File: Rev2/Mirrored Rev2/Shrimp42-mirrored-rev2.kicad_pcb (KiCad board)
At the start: 2 copper layers, 147.3 x 89 mm, 53 parts, among them J1 02x05, J2 02x05, U1 ProMicro, U2 trrs

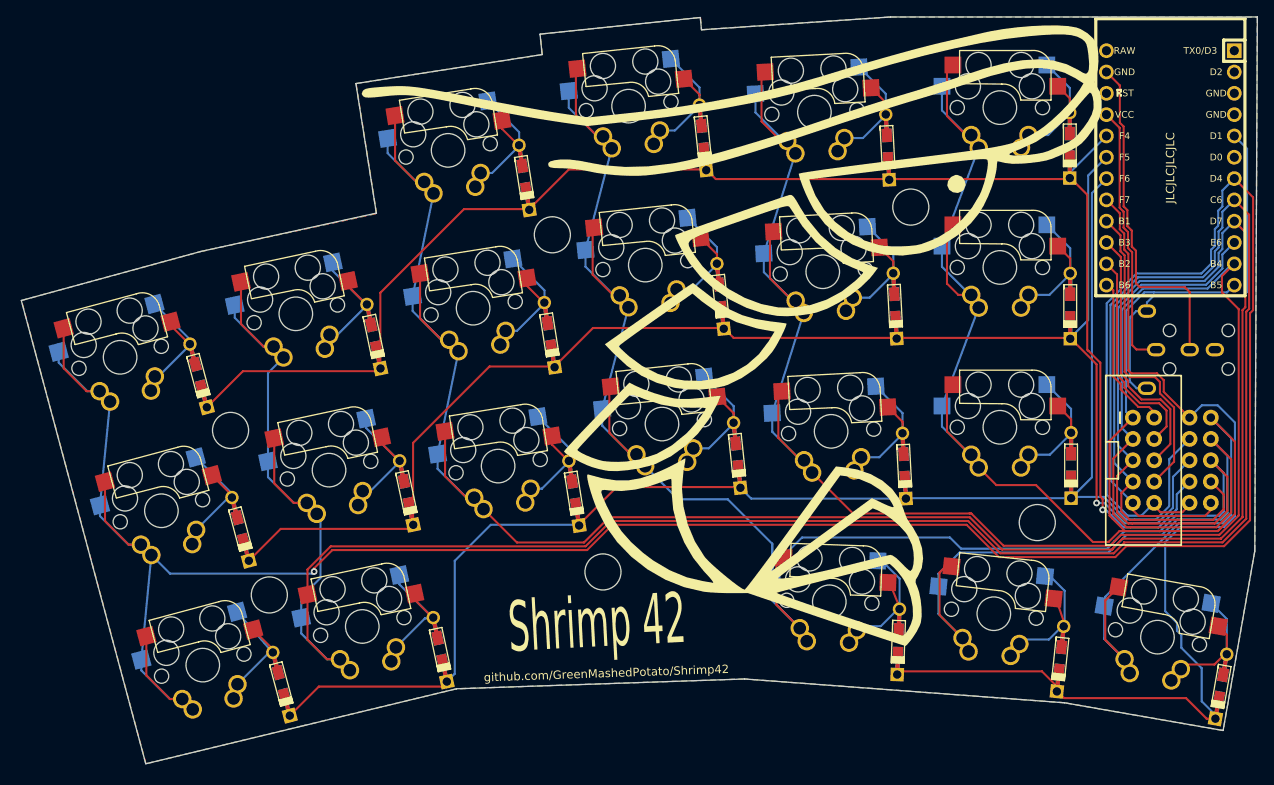
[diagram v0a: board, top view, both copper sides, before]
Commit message: update shrimp image to be smaller
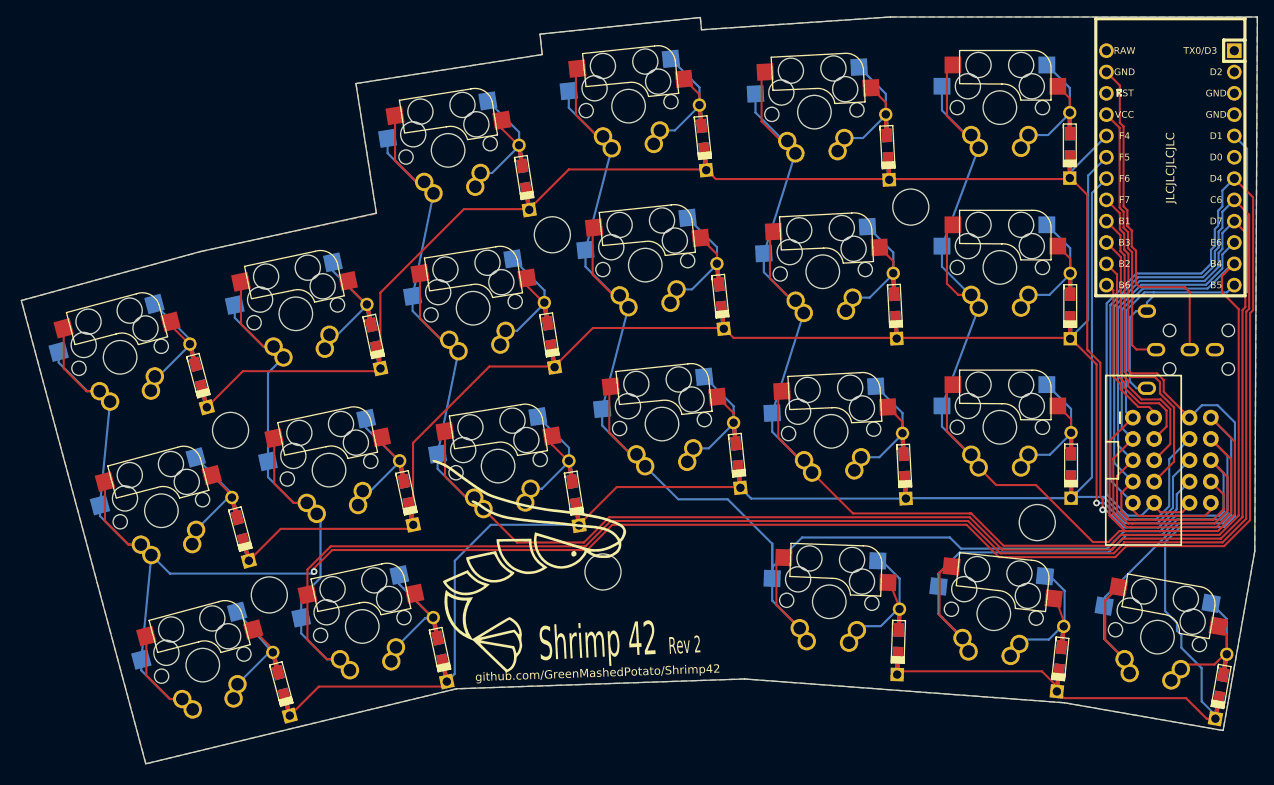
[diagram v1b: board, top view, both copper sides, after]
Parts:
- removed the G*** at (106.4, 65.2)
- added G***: LOGO, footprints:Shrimp_small_small, B.Cu at (71.5, 84.3)
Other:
- board text added: "Rev 2"

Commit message: update thumb cluster since its too close to amphenol cutout
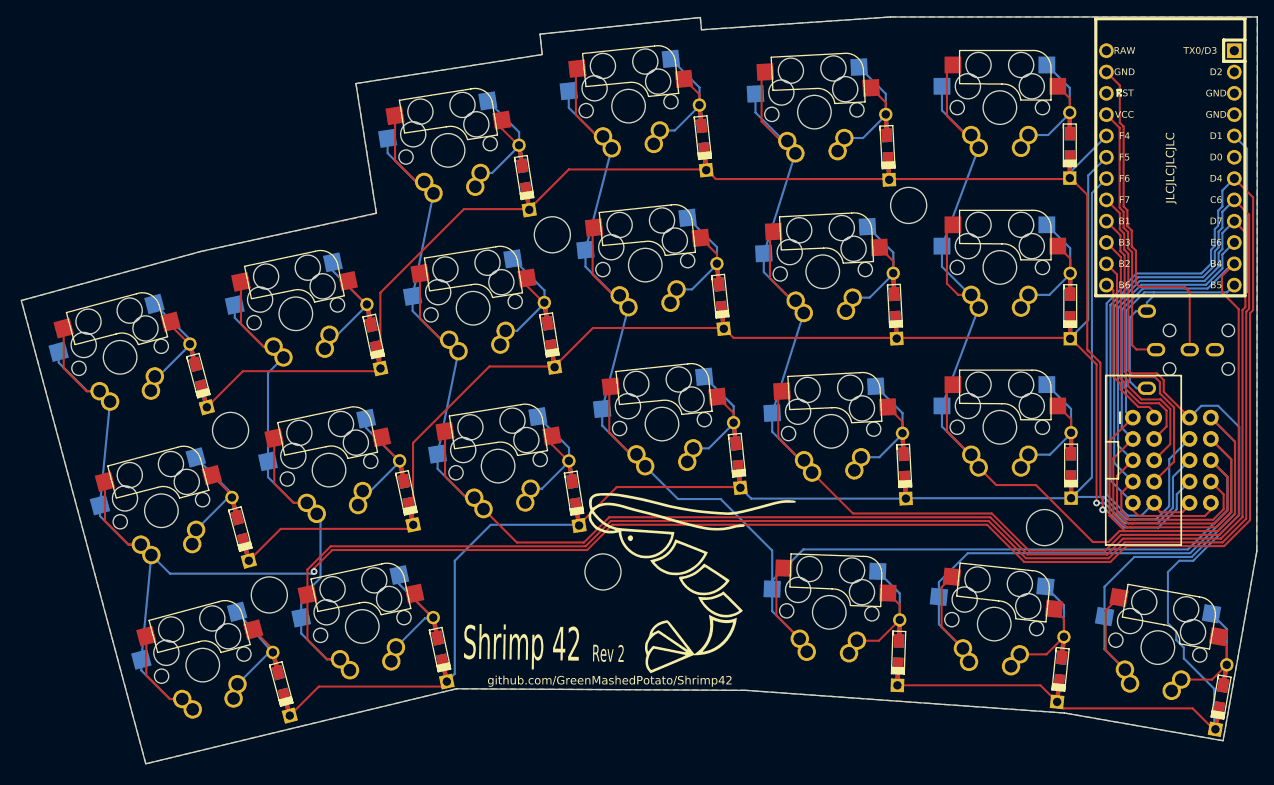
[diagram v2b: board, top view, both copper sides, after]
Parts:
- G***: moved to F.Cu
- moved G*** 21.7 mm to (93.2, 85.1), turned to -4 degrees
- moved D-3-3 1.28 mm to (118.7, 91.8)
- moved D-3-5 1.26 mm to (157.1, 97.1)
- moved K-3-3 1.26 mm to (110.4, 87.0)
- moved D-3-4 1.25 mm to (138.0, 93.8)
- moved K-3-5 1.24 mm to (149.6, 91.2)
- moved K-3-4 1.24 mm to (130.1, 88.4)
- moved Ref** 1.06 mm to (136.1, 76.9)
- moved Ref** 0.32 mm to (119.9, 38.5)
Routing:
- net CL3: track 247.7 -> 244.1 mm
- net CL5: track 216.2 -> 217.4 mm
- net CL4: track 293.2 -> 294.2 mm
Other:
- outline, holes or cut-outs redrawn

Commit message: update readme, update icon
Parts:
- removed the G*** at (93.2, 85.1)
- added G***: LOGO, footprints:shrimp-vector_med, F.Cu at (92.3, 89.0)

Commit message: rewired board. change pcb holes. push commit before order pcb
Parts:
- removed G***: LOGO, footprints:shrimp-vector_med
- Ref**1, Ref**2, Ref**3, Ref**4, Ref**5, Ref**6: renamed from Ref**; footprint footprintsGlobal:hole-m2-pcb -> footprints:HOLE_M2_TH
- moved D-2-0 0.70 mm to (44.6, 96.0)
- moved Ref**5 0.70 mm to (82.9, 82.7)
- moved K-0-0 0.70 mm to (25.4, 57.1)
- moved D-0-1 0.70 mm to (55.6, 54.6)
- moved D-0-5 0.70 mm to (138.6, 31.8)
- moved D-0-2 0.70 mm to (73.6, 35.6)
- moved D-2-4 0.70 mm to (118.9, 70.0)
- moved K-2-1 0.70 mm to (54.3, 89.2)
- moved D-0-0 0.70 mm to (34.7, 59.3)
- moved K-2-4 0.70 mm to (110.1, 65.9)
- moved D-3-5 0.70 mm to (156.6, 97.6)
- moved J1 0.70 mm to (147.4, 69.3)
- moved D-2-3 0.70 mm to (98.9, 68.7)
- moved K-3-3 0.70 mm to (109.9, 87.5)
- moved K-3-5 0.70 mm to (149.1, 91.7)
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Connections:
- U1 pad 3: unconnected-(U1-Pad3) -> GND
- U1 pad 4: unconnected-(U1-Pad4) -> GND
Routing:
- net CL4: track 294.2 -> 235.6 mm, vias 0 -> 1
- net GND: track 40.4 -> 52.4 mm, vias 0 -> 42
- net CL5: track 217.4 -> 225.9 mm
- net CL1: track 299.0 -> 292.6 mm
- net CL3: track 244.1 -> 250.2 mm, vias 0 -> 1
- net CL0: track 319.0 -> 314.1 mm
- net Net-(D-0-0-Pad2): track 14.6 -> 16.8 mm
- net Net-(D-1-0-Pad2): track 14.9 -> 17.0 mm
- net Net-(D-0-1-Pad2): track 15.0 -> 17.0 mm
- net Net-(D-1-1-Pad2): track 14.9 -> 16.9 mm
- net VCC: track 32.4 -> 30.5 mm
- net Net-(D-2-0-Pad2): track 15.1 -> 17.0 mm
- net RL2: track 174.9 -> 173.4 mm
- net Net-(D-2-1-Pad2): track 15.9 -> 17.1 mm
- net RL0: track 181.6 -> 182.5 mm
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- added copper zone on B.Cu, net GND
- added copper zone on F.Cu, net GND
- removed copper zone on B.Cu, net (none)
- removed copper zone on F.Cu, net (none)
